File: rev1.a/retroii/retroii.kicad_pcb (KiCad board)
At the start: 4 copper layers, 362 x 215.9 mm, 293 parts, among them CON1 SD_Card_SPI, J1 VGA, J10 BARREL_JACK, J11 Conn_02x10, J12 Peripheral Slot 0, J13 74LS74, J14 Game_IO_Socket, J15 Peripheral Slot 4, J16 Peripheral Slot 1, J17 Peripheral Slot 5, J18 Peripheral Slot 2, J19 Peripheral Slot 6, J2 DB9_Female_Stacked, J20 Peripheral Slot 3, J21 Peripheral Slot 7, J22 Conn_01x09, J23 Conn_01x02, J24 Headphone, J3 DB15_Female_Stacked, J6 Edge mounted connector, J7 Cassette In, J8 Cassette Out, J9 Speaker Jack, K1 PS2_KEYBOARD, K13 LM741, P1 PROP_PLUG, P2 PROP_PLUG, Q4 MPSA13, Q5 2N3904, SW1 SW_PUSH_SAFE, SW2 SPST2, SW3 SAVE, SW4 LOAD, SW5 SW_PUSH_SAFE, SW6 RESET, SW7 MISC1, SW8 MISC2, U1 74LS00, U10 74LS08, U11 LM2576-12, U12 LM2576-5, U13 LM2576-12, U14 LM2576-3.3, U15 LM2576-5, U16 Prop_P8X32A, U17 24LC256_EEPROM, U18 74LS04, U3 74LS11, U4 Prop_P8X32A, U5 24LC256_EEPROM, U6 AT28C256_EEPROM, U8 IDT7008_Dual_Port_RAM, U9 74LS32, Y1 5MHz 20pf, Y2 ECS-2100X-1MHZ, Y3 5MHz 20pf

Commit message: laying out audio
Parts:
- removed R56, R57, R67: 1K, retroii_footprints:R_Axial_DIN0207_L6.3mm_D2.5mm_P10.16mm_Horizontal
- added RA2: 1K R_Network, Resistor_THT:R_Array_SIP4, F.Cu at (344.2, 323.5)
- moved R17 256.5 mm to (387.2, 345.5), turned to 90 degrees
- moved R16 253.7 mm to (369.8, 332.0)
- moved R15 223.9 mm to (367.0, 335.5), turned to 270 degrees
- moved C12 212.9 mm to (319.2, 331.2)
- moved J9 206.8 mm to (349.8, 348.5), turned to 90 degrees
- moved C42 187.9 mm to (343.2, 328.2)
- moved J6 48.4 mm to (292.8, 309.0)
- moved C10 30.0 mm to (386.0, 351.8), turned to 0 degrees
- moved R29 21.0 mm to (364.0, 345.8)
- moved R30 20.5 mm to (384.2, 345.5)
- moved R18 19.0 mm to (380.8, 351.5)
- moved R19 19.0 mm to (380.8, 348.5)
- moved D5 15.2 mm to (250.8, 292.0), turned to 180 degrees
- moved R25 10.8 mm to (325.8, 328.2), turned to 0 degrees
- moved CR1 10.5 mm to (356.8, 328.2), turned to 180 degrees
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
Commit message: layout mods for serial io
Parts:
- J6: footprint Connector_PinSocket_2.54mm:PinSocket_2x07_P2.54mm_Horizontal -> retroii_footprints:PinSocket_2x08_P2.54mm_Vertical
- moved C43 228.7 mm to (376.2, 329.0), turned to 180 degrees
- moved R23 210.9 mm to (331.0, 327.2)
- moved R20 209.1 mm to (313.2, 326.5)
- moved C75 197.3 mm to (327.8, 315.8), turned to 90 degrees
- moved R22 196.3 mm to (344.5, 303.5), turned to 270 degrees
- moved C79 194.9 mm to (334.2, 322.8), turned to 180 degrees
- moved C7 193.8 mm to (327.8, 321.0), turned to 90 degrees
- moved C74 192.0 mm to (339.0, 298.2), turned to 180 degrees
- moved C6 187.4 mm to (344.2, 319.5), turned to 90 degrees
- moved R68 185.9 mm to (322.2, 298.5)
- moved C77 183.7 mm to (337.2, 322.8)
- moved C8 181.8 mm to (321.2, 322.8)
- moved C9 178.9 mm to (317.8, 322.8), turned to 180 degrees
- moved JP11 173.0 mm to (299.8, 338.8), turned to 180 degrees
- moved C78 170.5 mm to (327.8, 307.5), turned to 270 degrees
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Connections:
- J6 pad 11: /Serial_IO_Audio/PDL0 -> /Serial_IO_Audio/PDL3
- J6 pad 12: /Serial_IO_Audio/PB0 -> /Address_Decoding/SS_AN3_OFF_ON
- J6 pad 13: /Serial_IO_Audio/PB1 -> /Address_Decoding/SS_AN2_OFF_ON
- J6 pad 14: /Serial_IO_Audio/PB2 -> /Address_Decoding/SS_AN1_OFF_ON
- J6 pad 2: /Address_Decoding/SS_AN0_OFF_ON -> /Serial_IO_Audio/PB0
- J6 pad 3: /Address_Decoding/SS_AN1_OFF_ON -> /Serial_IO_Audio/PB1
- J6 pad 4: /Address_Decoding/SS_AN2_OFF_ON -> /Serial_IO_Audio/PB2
- J6 pad 5: /Address_Decoding/SS_AN3_OFF_ON -> /Address_Decoding/C040_Strobe
- J6 pad 6: /Address_Decoding/C040_Strobe -> /Serial_IO_Audio/PDL0
- J6 pad 7: GND -> /Serial_IO_Audio/PDL2
- J6 pad 8: /Serial_IO_Audio/PDL3 -> GND
- J6 pad 9: /Serial_IO_Audio/PDL2 -> Net-(J6-Pad9)

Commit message: finished initial layout
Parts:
- moved C53 360.9 mm to (458.5, 357.0), turned to 0 degrees
- moved C54 328.7 mm to (458.5, 305.0), turned to 0 degrees
- moved C50 325.6 mm to (458.2, 277.8), turned to 0 degrees
- moved C47 313.6 mm to (461.0, 226.0), turned to 180 degrees
- moved C49 308.0 mm to (443.5, 252.8), turned to 180 degrees
- moved R1 306.2 mm to (465.0, 251.0), turned to 180 degrees
- moved JP1 303.5 mm to (468.2, 258.8)
- moved C48 288.7 mm to (426.2, 226.0), turned to 180 degrees
- moved C52 280.3 mm to (443.5, 225.8)
- moved C18 252.8 mm to (378.2, 280.5)
- moved C43 4.03 mm to (375.8, 325.0)
- moved C51 0.75 mm to (458.5, 331.2)

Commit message: working on optimizing keyboard layout
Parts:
- moved C47 115.9 mm to (421.0, 334.8)
- moved U1 115.9 mm to (416.0, 338.2)
- moved R28 114.3 mm to (415.2, 235.8)
- moved C53 110.9 mm to (423.5, 251.8)
- moved F14 110.9 mm to (428.5, 248.2)
- moved C52 107.7 mm to (459.5, 332.2)
- moved F12 107.7 mm to (454.5, 336.0)
- moved C48 107.1 mm to (439.5, 332.2)
- moved H1 107.1 mm to (434.2, 335.8)
- moved C39 83.4 mm to (464.0, 258.0)
- moved JP6 83.4 mm to (454.0, 267.5)
- moved U9 83.4 mm to (459.0, 262.5)
- moved C51 81.5 mm to (440.8, 251.8)
- moved F13 81.5 mm to (445.8, 248.0)
- moved C40 75.8 mm to (443.2, 256.2)
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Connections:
- R69 pad 2: /Address_Decoding/SS_GRAPHICS_TEXT -> /Address_Decoding/SS_LORES_HIRES
- R70 pad 2: /Address_Decoding/SS_NOMIX_MIX -> /Address_Decoding/SS_PAGE1_PAGE2
- R71 pad 2: /Address_Decoding/SS_PAGE1_PAGE2 -> /Address_Decoding/SS_NOMIX_MIX
- R72 pad 2: /Address_Decoding/SS_LORES_HIRES -> /Address_Decoding/SS_GRAPHICS_TEXT

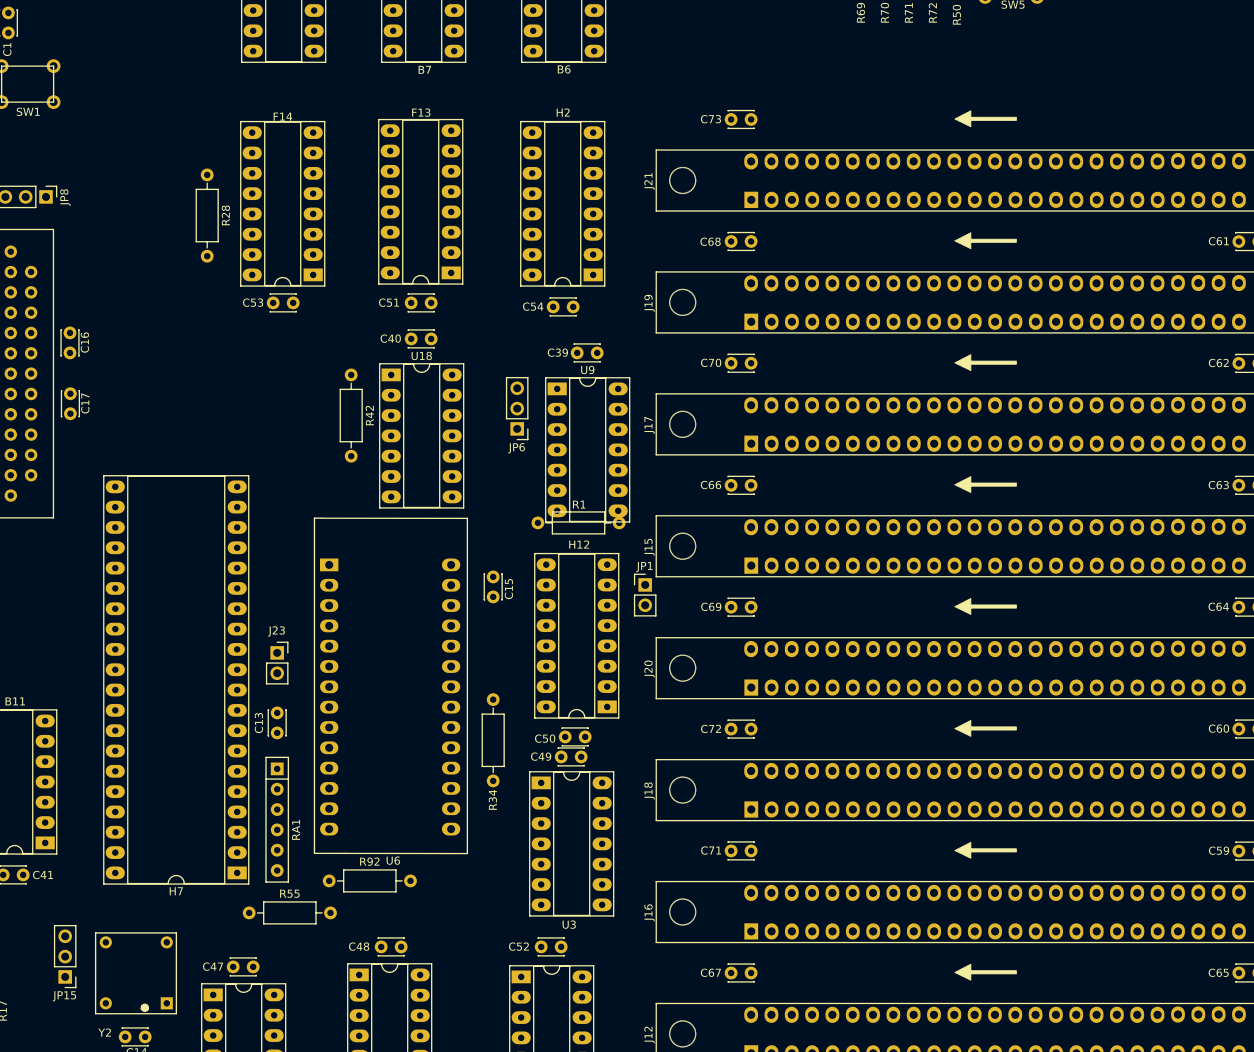
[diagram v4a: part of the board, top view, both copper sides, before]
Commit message: modified prop layout to include jumpers for phi2, rdy, and dma.
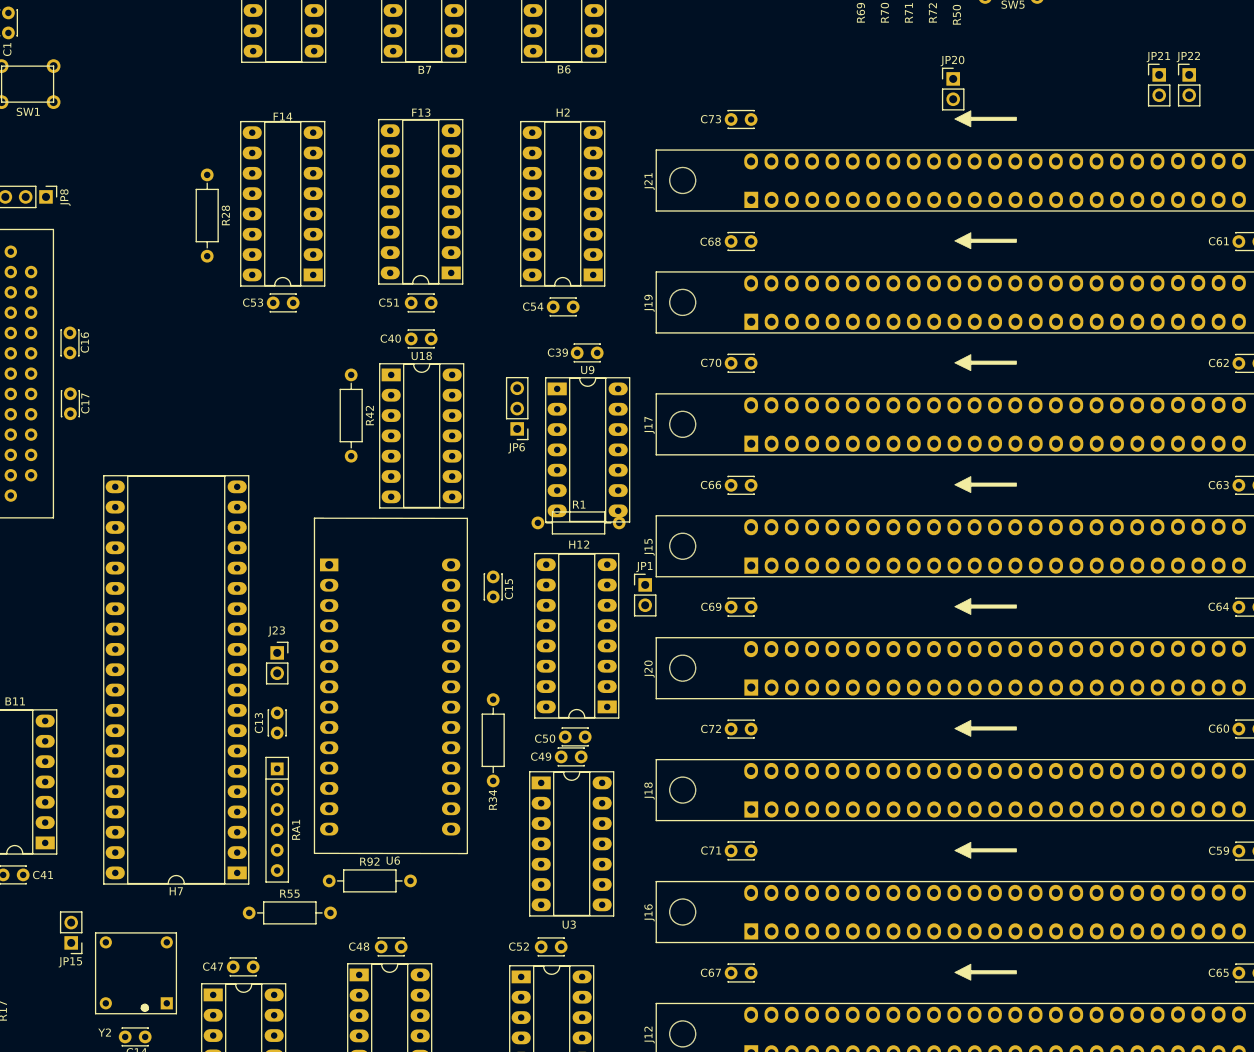
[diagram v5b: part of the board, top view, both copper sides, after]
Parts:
- added JP20: Jumper_NO_Small, Connector_PinHeader_2.54mm:PinHeader_1x02_P2.54mm_Vertical, F.Cu at (508.5, 223.8)
- added JP21: Jumper_NO_Small, Connector_PinHeader_2.54mm:PinHeader_1x02_P2.54mm_Vertical, F.Cu at (534.2, 223.2)
- added JP22: Jumper_NO_Small, Connector_PinHeader_2.54mm:PinHeader_1x02_P2.54mm_Vertical, F.Cu at (538.0, 223.2)
- JP15: value Jumper_3_Open -> Jumper; footprint Connector_PinHeader_2.54mm:PinHeader_1x03_P2.54mm_Vertical -> Connector_PinHeader_2.54mm:PinHeader_1x02_P2.54mm_Vertical
- moved JP15 4.32 mm to (398.2, 331.8)
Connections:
- J22 pad 1: /CPU_RAM_ROM/Prop_PHI2 -> Net-(J22-Pad1)
- J22 pad 2: /Peripheral_IO/Prop_7M -> Net-(J22-Pad2)
- J22 pad 3: /Peripheral_IO/Prop_Q3 -> /Peripheral_IO/Prop_7M
- J22 pad 4: Net-(J22-Pad4) -> /Peripheral_IO/Prop_Q3
- JP15 pad 1: /CPU_RAM_ROM/Prop_PHI2 -> /CPU_RAM_ROM/Clock
- U16 pad 18: Net-(J22-Pad4) -> /Peripheral_IO/Prop_Q3
- U16 pad 19: /Peripheral_IO/Prop_Q3 -> /Peripheral_IO/Prop_7M
- U16 pad 20: /Peripheral_IO/Prop_7M -> Net-(J22-Pad2)
- U16 pad 21: /CPU_RAM_ROM/Prop_PHI2 -> Net-(J22-Pad1)

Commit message: updated strobe/reset/keyboard connections
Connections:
- C36 pad 2: /Power_Supply/+3V3 -> Net-(C36-Pad2)
- R73 pad 1: /SD_Card_And_Keyboard/K0 -> /SD_Card_And_Keyboard/Strobe
- R74 pad 1: /SD_Card_And_Keyboard/K1 -> /CPU_RAM_ROM/RESB
- R75 pad 1: /SD_Card_And_Keyboard/K2 -> /SD_Card_And_Keyboard/K6
- R76 pad 1: /SD_Card_And_Keyboard/K3 -> /SD_Card_And_Keyboard/K5
- R78 pad 1: /SD_Card_And_Keyboard/K5 -> /SD_Card_And_Keyboard/K3
- R79 pad 1: /SD_Card_And_Keyboard/K6 -> /SD_Card_And_Keyboard/K2
- R80 pad 1: /CPU_RAM_ROM/RESB -> /SD_Card_And_Keyboard/K1
- R81 pad 1: /SD_Card_And_Keyboard/Strobe -> /SD_Card_And_Keyboard/K0
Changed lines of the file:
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@@
     (zones 0)
     (modules 294)
-    (nets 364)
+    (nets 365)
   )
   (page A2)
@@
   (net 362 "Net-(J22-Pad1)")
   (net 363 "Net-(J22-Pad2)")
+  (net 364 "Net-(C36-Pad2)")
   (net_class Default "This is the default net class."
     (clearance 0.2)
@@
     (add_net "Net-(C30-Pad1)")
     (add_net "Net-(C31-Pad2)")
+    (add_net "Net-(C36-Pad2)")
     (add_net "Net-(C38-Pad1)")
     (add_net "Net-(C38-Pad2)")
@@
     (fp_line (start -0.25 -1) (end -0.25 1) (layer F.Fab) (width 0.1))
     (pad 2 thru_hole circle (at 2.5 0 270) (size 1.6 1.6) (drill 0.8) (layers *.Cu *.Mask)
-      (net 46 /Power_Supply/+3V3))
+      (net 364 "Net-(C36-Pad2)"))
     (pad 1 thru_hole circle (at 0 0 270) (size 1.6 1.6) (drill 0.8) (layers *.Cu *.Mask)
       (net 2 GND))
@@
       (net 328 "Net-(R73-Pad2)"))
     (pad 1 thru_hole circle (at 0 0 270) (size 1.6 1.6) (drill 0.8) (layers *.Cu *.Mask)
-      (net 9 /SD_Card_And_Keyboard/K0))
+      (net 14 /SD_Card_And_Keyboard/Strobe))
     (model ${KISYS3DMOD}/Resistor_THT.3dshapes/R_Axial_DIN0207_L6.3mm_D2.5mm_P10.16mm_Horizontal.wrl
       (at (xyz 0 0 0))
@@
       (net 329 "Net-(R74-Pad2)"))
     (pad 1 thru_hole circle (at 0 0 270) (size 1.6 1.6) (drill 0.8) (layers *.Cu *.Mask)
-      (net 7 /SD_Card_And_Keyboard/K1))
+      (net 12 /CPU_RAM_ROM/RESB))
     (model ${KISYS3DMOD}/Resistor_THT.3dshapes/R_Axial_DIN0207_L6.3mm_D2.5mm_P10.16mm_Horizontal.wrl
       (at (xyz 0 0 0))
@@
       (net 330 "Net-(R75-Pad2)"))
     (pad 1 thru_hole circle (at 0 0 270) (size 1.6 1.6) (drill 0.8) (layers *.Cu *.Mask)
-      (net 13 /SD_Card_And_Keyboard/K2))
+      (net 4 /SD_Card_And_Keyboard/K6))
     (model ${KISYS3DMOD}/Resistor_THT.3dshapes/R_Axial_DIN0207_L6.3mm_D2.5mm_P10.16mm_Horizontal.wrl
       (at (xyz 0 0 0))
@@
     )
     (pad 1 thru_hole circle (at 0 0 270) (size 1.6 1.6) (drill 0.8) (layers *.Cu *.Mask)
-      (net 11 /SD_Card_And_Keyboard/K3))
+      (net 8 /SD_Card_And_Keyboard/K5))
     (pad 2 thru_hole oval (at 10.16 0 270) (size 1.6 1.6) (drill 0.8) (layers *.Cu *.Mask)
       (net 331 "Net-(R76-Pad2)"))
@@
       (net 333 "Net-(R78-Pad2)"))
     (pad 1 thru_hole circle (at 0 0 270) (size 1.6 1.6) (drill 0.8) (layers *.Cu *.Mask)
-      (net 8 /SD_Card_And_Keyboard/K5))
+      (net 11 /SD_Card_And_Keyboard/K3))
     (model ${KISYS3DMOD}/Resistor_THT.3dshapes/R_Axial_DIN0207_L6.3mm_D2.5mm_P10.16mm_Horizontal.wrl
       (at (xyz 0 0 0))
@@
       (net 334 "Net-(R79-Pad2)"))
     (pad 1 thru_hole circle (at 0 0 270) (size 1.6 1.6) (drill 0.8) (layers *.Cu *.Mask)
-      (net 4 /SD_Card_And_Keyboard/K6))
+      (net 13 /SD_Card_And_Keyboard/K2))
     (model ${KISYS3DMOD}/Resistor_THT.3dshapes/R_Axial_DIN0207_L6.3mm_D2.5mm_P10.16mm_Horizontal.wrl
       (at (xyz 0 0 0))
@@
     )
     (pad 1 thru_hole circle (at 0 0 270) (size 1.6 1.6) (drill 0.8) (layers *.Cu *.Mask)
-      (net 12 /CPU_RAM_ROM/RESB))
+      (net 7 /SD_Card_And_Keyboard/K1))
     (pad 2 thru_hole oval (at 10.16 0 270) (size 1.6 1.6) (drill 0.8) (layers *.Cu *.Mask)
       (net 335 "Net-(R80-Pad2)"))
@@
     )
     (pad 1 thru_hole circle (at 0 0 270) (size 1.6 1.6) (drill 0.8) (layers *.Cu *.Mask)
-      (net 14 /SD_Card_And_Keyboard/Strobe))
+      (net 9 /SD_Card_And_Keyboard/K0))
     (pad 2 thru_hole oval (at 10.16 0 270) (size 1.6 1.6) (drill 0.8) (layers *.Cu *.Mask)
       (net 336 "Net-(R81-Pad2)"))

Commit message: keyboard/sd card propeller circuitry more or less in final position
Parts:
- moved C39 20.7 mm to (443.5, 255.5)
- moved JP6 20.7 mm to (433.5, 265.0)
- moved U9 20.7 mm to (438.5, 260.0)
- moved C40 19.0 mm to (462.2, 255.2)
- moved R42 19.0 mm to (452.2, 259.8)
- moved U18 19.0 mm to (457.2, 259.8)
- moved J6 17.8 mm to (287.0, 304.0), turned to 0 degrees
- moved SW6 15.0 mm to (495.0, 154.0)
- moved R59 7.65 mm to (515.6, 158.0)
- moved R63 7.65 mm to (515.6, 161.0)
- moved SW4 7.25 mm to (514.0, 154.0)
- moved R60 4.90 mm to (534.6, 158.0)
- moved R64 4.90 mm to (534.6, 161.0)
- moved SW3 4.50 mm to (533.0, 154.0)
- moved R73 1.92 mm to (496.1, 167.2)
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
